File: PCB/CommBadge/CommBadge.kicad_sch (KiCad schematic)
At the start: 46 parts, among them J1 Battery, J2 Reset, J3 TC2030-USB-NL-DS, J4 TF_PUSH, J5 USB-C-Socket-H, Q2 CJ2301, SW1 SW_Push, U1 R, U2 ESP32-S3-MINI-1, U2 L, U3 TP4054, U4 ME6211C33M5G-N

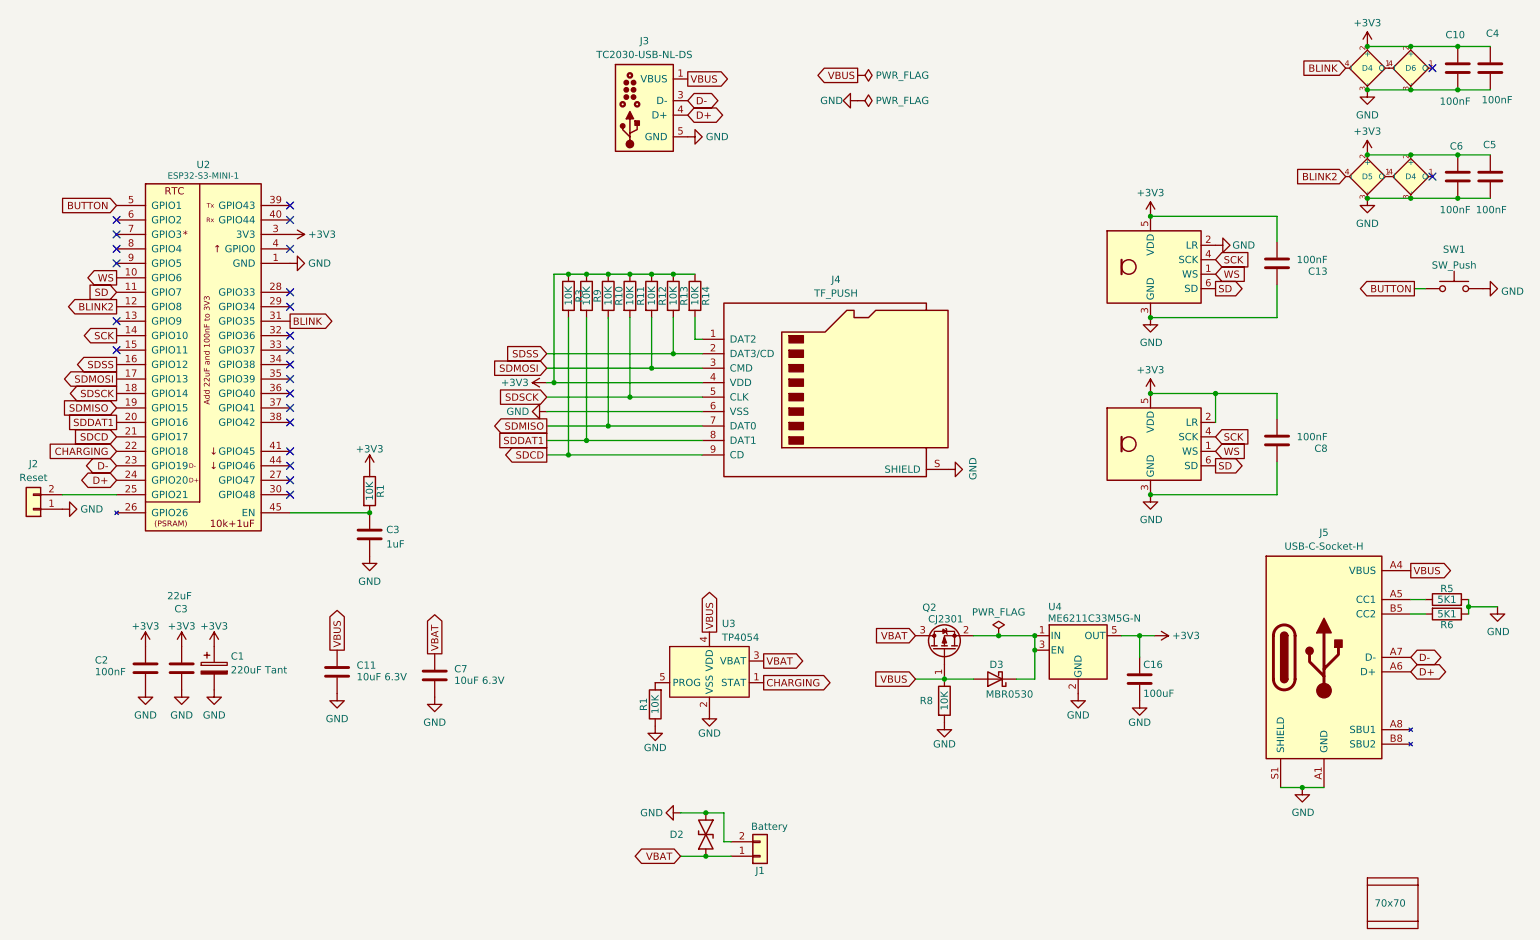
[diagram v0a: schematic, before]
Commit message: Moved LEDs
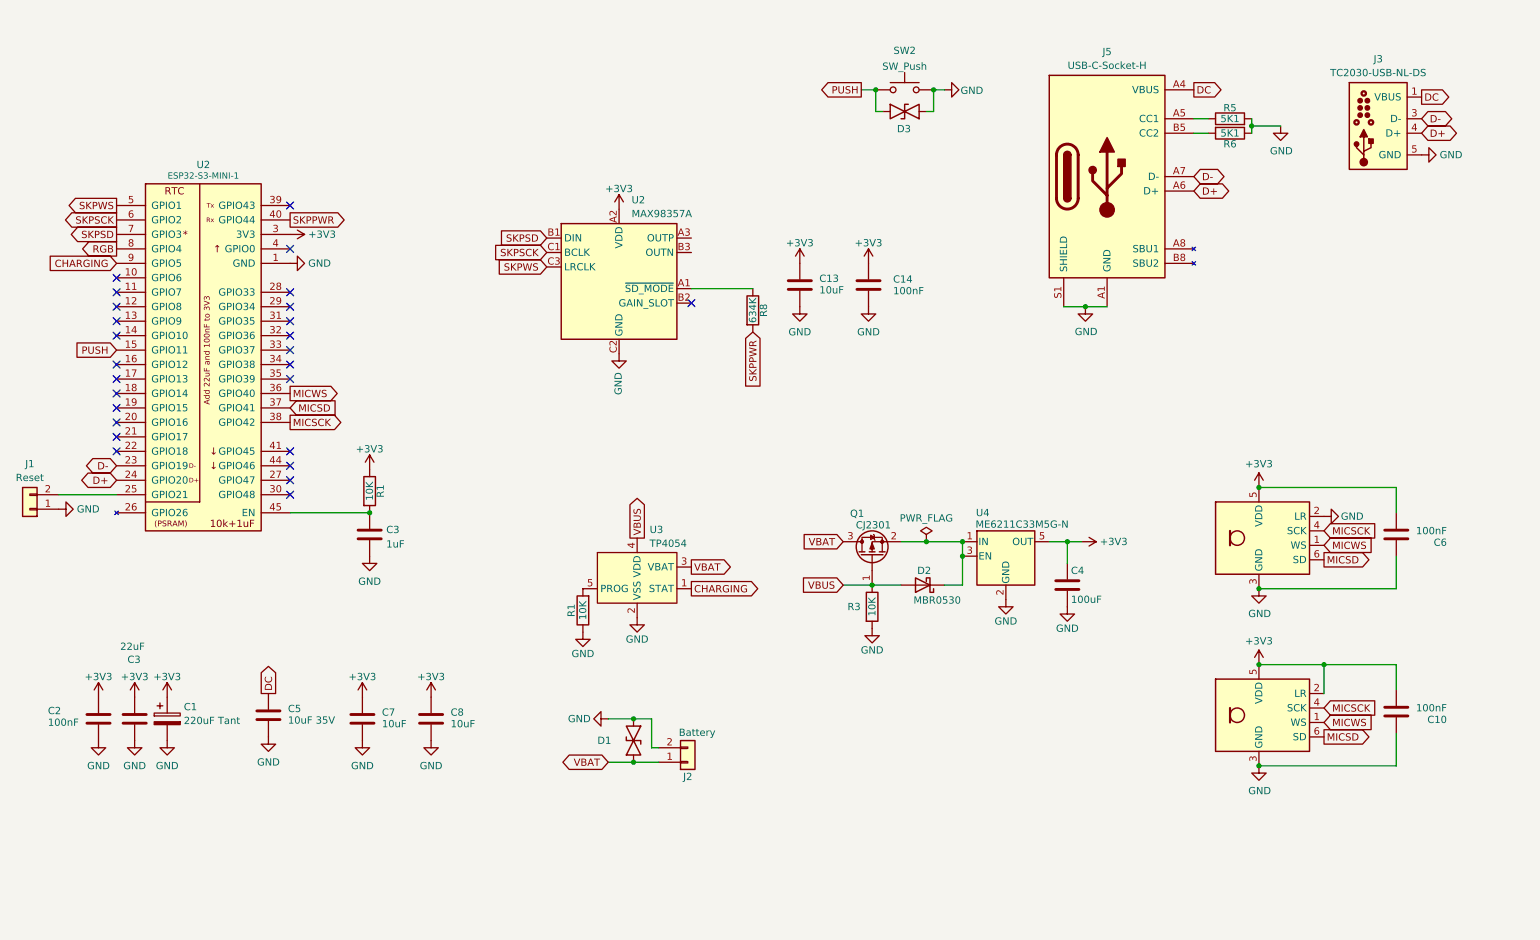
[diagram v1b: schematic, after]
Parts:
- removed C11: 10uF 6.3V, RevK:C_0402, symbol Device:C
- removed C16: 100uF, RevK:C_0805, symbol Device:C
- removed D2: ~, RevK:DFN1006-2L, symbol RevK:ES05D1MC10
- removed D3: MBR0530, RevK:D_SOD-123, symbol Device:D_Schottky
- removed D4 (x2), D5, D6: XL-1010RGBC-WS2812B, RevK:SMD1010, symbol RevK:WS2812B-1mm
- removed J4: TF_PUSH, RevK:TF_PUSH, symbol RevK:TF_PUSH
- removed PCB1: 70x70, RevK:PCB7070, symbol RevK:PCB
- removed Q2: CJ2301, RevK:SOT-23, symbol Transistor_FET:BSS83P
- removed R10, R11, R12, R13, R14, R9: 10K, RevK:R_0402, symbol Device:R
- removed SW1: SW_Push, RevK:TS-1092S-B3D2-G, symbol Switch:SW_Push
- removed U1: R, RevK:ICS43434_MEMS_Mic, symbol RevK:ICS43434_MEMS_Mic
- removed U2: L, RevK:ICS43434_MEMS_Mic, symbol RevK:ICS43434_MEMS_Mic
- removed V1, V2: ~, RevK:VCUT70N, symbol RevK:VCUT
- added C14: 100nF, RevK:C_0402, symbol Device:C
- added D1, D3: ~, RevK:DFN1006-2L, symbol RevK:ES05D1MC10
- added D2: MBR0530, RevK:D_SOD-123, symbol Device:D_Schottky
- added Q1: CJ2301, RevK:SOT-23, symbol Transistor_FET:BSS83P
- added SW2: SW_Push, RevK:TS-1092S-B3D2-G, symbol Switch:SW_Push
- added U2: MAX98357A, RevK:WLP-1.437mmx1.347mm-0.21mm-ball, symbol RevK:MAX98357A
- added U5: L, RevK:ICS43434_MEMS_Mic_Open, symbol RevK:ICS43434_MEMS_Mic
- added U7: R, RevK:ICS43434_MEMS_Mic_Open, symbol RevK:ICS43434_MEMS_Mic
- C13, C8: value 100nF -> 10uF; LCSC Part # (none) -> C15525
- C4: value 100nF -> 100uF; footprint RevK:C_0402 -> RevK:C_0805; LCSC Part # (none) -> C141660
- C5: value 100nF -> 10uF 35V; footprint RevK:C_0402 -> RevK:C_0603; LCSC Part # (none) -> C194427
- C7: value 10uF 6.3V -> 10uF; LCSC Part # C194427 -> C15525
- J1: value Battery -> Reset; footprint RevK:1.25T-2PWT (Molex 532610271) -> RevK:AA-Pad; LCSC Part # C177225 -> (none); now left out of the parts list
- J2: value Reset -> Battery; footprint RevK:AA-Pad -> RevK:1.25T-2PWT (Molex 532610271); LCSC Part # (none) -> C177225; now in the parts list
- R8: value 10K -> 634K
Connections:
- net +3V3: now also C10.2, C13.1, C6.2, C7.1, C8.1, C14.1, U2.A2 (VDD), U5.5 (VDD), U7.2 (LR), U7.5 (VDD); no longer C10.1, C13.2, C5.1, C6.1, C8.2, R3.1
- net CHARGING: now also U2.9 (GPIO5); no longer U2.22 (GPIO18)
- net GND: now also C10.1, C13.2, C6.1, C8.2, J1.1 (Pin_1), J2.2 (Pin_2), R3.2, C14.2, D1.1, D3.1, SW2.1, U2.C2 (GND), U5.2 (LR), U5.3 (GND), U7.3 (GND); no longer C10.2, C13.1, C6.2, C8.1, J1.2 (Pin_2), J2.1 (Pin_1), R8.2
- net VBAT: now also J2.1 (Pin_1), D1.2, Q1.3 (D); no longer C7.1, J1.1 (Pin_1)
- net VBUS: now also R3.1, D2.2 (A), Q1.1 (G); no longer J3.1 (VBUS), J3.2 (VBUS), J5.A4 (VBUS), J5.A9 (VBUS), J5.B4 (VBUS), J5.B9 (VBUS), R8.1
- net at U4.1 (IN), U4.3 (EN): now also D2.1 (K), Q1.2 (S)
- net PUSH: now reaches U2.15 (GPIO11)
- net PUSH: now also D3.2, SW2.2
- net at U2.25 (GPIO21): now also J1.2 (Pin_2); no longer J2.2 (Pin_2)
- net MICWS: now reaches U2.36 (GPIO40)
- net MICWS: now also U5.1 (WS), U7.1 (WS)
- net MICSD: now reaches U2.37 (GPIO41)
- net MICSD: now also U5.6 (SD), U7.6 (SD)
- net MICSCK: now reaches U2.38 (GPIO42)
- net MICSCK: now also U5.4 (SCK), U7.4 (SCK)
- net SKPPWR: now reaches U2.40 (GPIO44)
- net SKPPWR: now also R8.2
- net SKPSCK: now reaches U2.6 (GPIO2)
- net SKPSCK: now also U2.C1 (BCLK)
- net SKPSD: now reaches U2.7 (GPIO3)
- net SKPSD: now also U2.B1 (DIN)
- net RGB: now reaches U2.8 (GPIO4)
- net BLINK: no longer names the net of U2.31 (GPIO35)
- net BLINK2: no longer names the net of U2.12 (GPIO8)
- net BUTTON renamed SKPWS
- net SKPWS: now also U2.C3 (LRCLK)
- net SCK: no longer names the net of U2.14 (GPIO10)
- net SD: no longer names the net of U2.11 (GPIO7)
- net SDCD: no longer names the net of U2.21 (GPIO17)
- net SDCD: no longer R3.2
- net SDDAT1: no longer names the net of U2.20 (GPIO16)
- net SDMISO: no longer names the net of U2.19 (GPIO15)
- net SDMOSI: no longer names the net of U2.17 (GPIO13)
- net SDSCK: no longer names the net of U2.18 (GPIO14)
- net SDSS: no longer names the net of U2.16 (GPIO12)
- net WS: no longer names the net of U2.10 (GPIO6)
- new net: R8.1, U2.A1 (~{SD_MODE})
- new net DC: C5.1, J3.1 (VBUS), J3.2 (VBUS), J5.A4 (VBUS), J5.A9 (VBUS), J5.B4 (VBUS), J5.B9 (VBUS)
- no-connect marks 24 -> 26
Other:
- title: Audio -> LED driver
- moved on the sheet: C1, C2, C3, J3, J5, R5, R6

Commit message: STart logci
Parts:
- added C11, C12, C15, C16, C17, C18: 100nF, RevK:C_0402, symbol Device:C
- added D4, D5, D6, D7, D8, D9: XL-1010RGBC-WS2812B, RevK:SMD1010, symbol RevK:WS2812B-1mm
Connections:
- net RGB: now also U2.10 (GPIO6), D4.4 (I)
- new net: C11.1, C12.1, C15.1, C16.1, C17.1, C18.1, D4.2 (+), D5.2 (+), D6.2 (+), D7.2 (+), D8.2 (+), D9.2 (+)
- new net: C11.2, C12.2, C15.2, C16.2, C17.2, C18.2, D4.3 (-), D5.3 (-), D6.3 (-), D7.3 (-), D8.3 (-), D9.3 (-)
- new net: D4.1 (O), D5.4 (I)
- new net: D6.1 (O), D7.4 (I)
- new net: D5.1 (O), D6.4 (I)
- new net: D7.1 (O), D8.4 (I)
- new net: D8.1 (O), D9.4 (I)

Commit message: Components
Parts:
- added LS1: Speaker, RevK:KLJ-Speaker, symbol Device:Speaker
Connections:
- net DC is gone; now on net VBUS: C5.1, J3.1 (VBUS), J3.2 (VBUS), J5.A4 (VBUS), J5.A9 (VBUS), J5.B4 (VBUS), J5.B9 (VBUS)
- net +3V3: now also C11.1, C12.1, C15.1, C16.1, C17.1, C18.1, D4.2 (+), D5.2 (+), D6.2 (+), D7.2 (+), D8.2 (+), D9.2 (+)
- net GND: now also C11.2, C12.2, C15.2, C16.2, C17.2, C18.2, D4.3 (-), D5.3 (-), D6.3 (-), D7.3 (-), D8.3 (-), D9.3 (-)
- net at U2.A3 (OUTP): now also LS1.1
- net at U2.B3 (OUTN): now also LS1.2

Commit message: Tweak
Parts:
- added R4: 10K, RevK:R_0402, symbol Device:R
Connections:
- net CHARGING: now also U2.17 (GPIO13); no longer U2.9 (GPIO5)
- net GND: now also U2.B2 (GAIN_SLOT)
- net PUSH: now also U2.16 (GPIO12); no longer U2.15 (GPIO11)
- net RGB: now also D9.4 (I), U2.5 (GPIO1); no longer D4.4 (I), U2.10 (GPIO6), U2.8 (GPIO4)
- net SKPPWR: now also U2.12 (GPIO8); no longer U2.40 (GPIO44)
- net SKPSCK: now also U2.21 (GPIO17); no longer U2.6 (GPIO2)
- net SKPSD: now also U2.22 (GPIO18); no longer U2.7 (GPIO3)
- net SKPWS: now also U2.20 (GPIO16); no longer U2.5 (GPIO1)
- net VBUS: now also R4.1
- net at D6.4 (I): now also D8.1 (O); no longer D5.1 (O)
- net at U2.19 (GPIO15): now also R4.2
- net at D7.1 (O): no longer D8.4 (I)
- net at D9.1 (O): now also D4.4 (I)
- new net: D5.1 (O), D8.4 (I)
- no-connect marks 26 -> 25
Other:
- moved on the sheet: D4, D5, D6, D7, D8, D9
